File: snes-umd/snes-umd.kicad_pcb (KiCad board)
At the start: 2 copper layers, 20.3 x 96 mm, 4 parts, among them CON101 UMDv3-CONN, CON102 SNES-CONN, U101 MCP23008T-E_SS

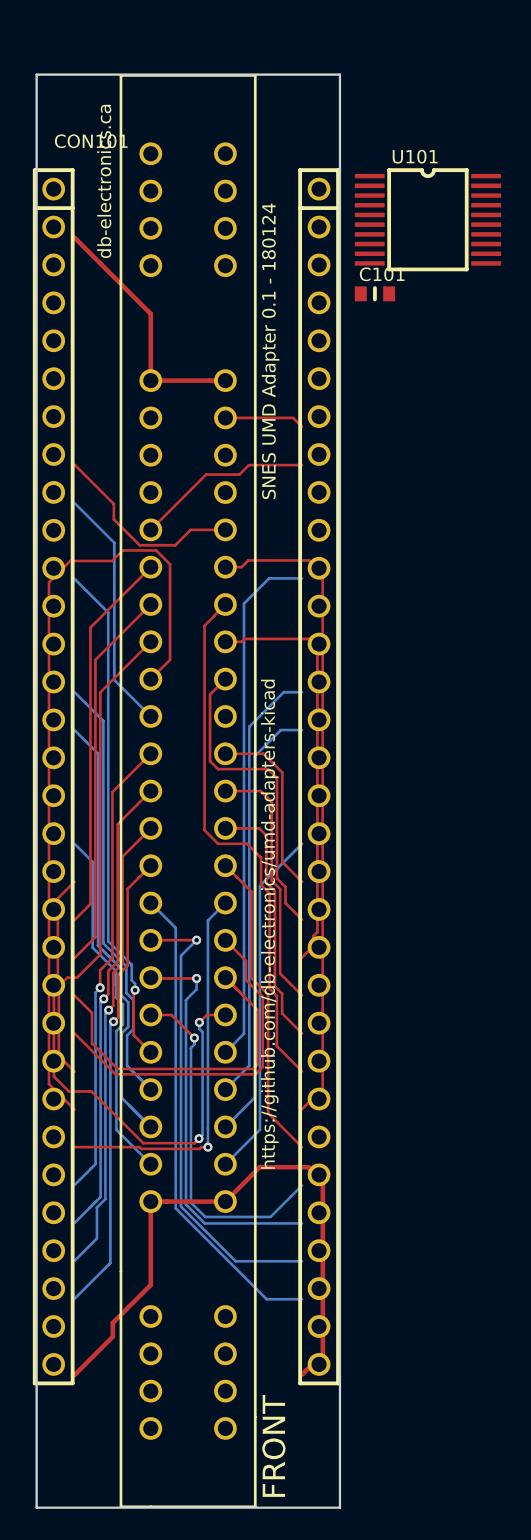
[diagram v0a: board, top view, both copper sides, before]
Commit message: board outline and sch mostly done
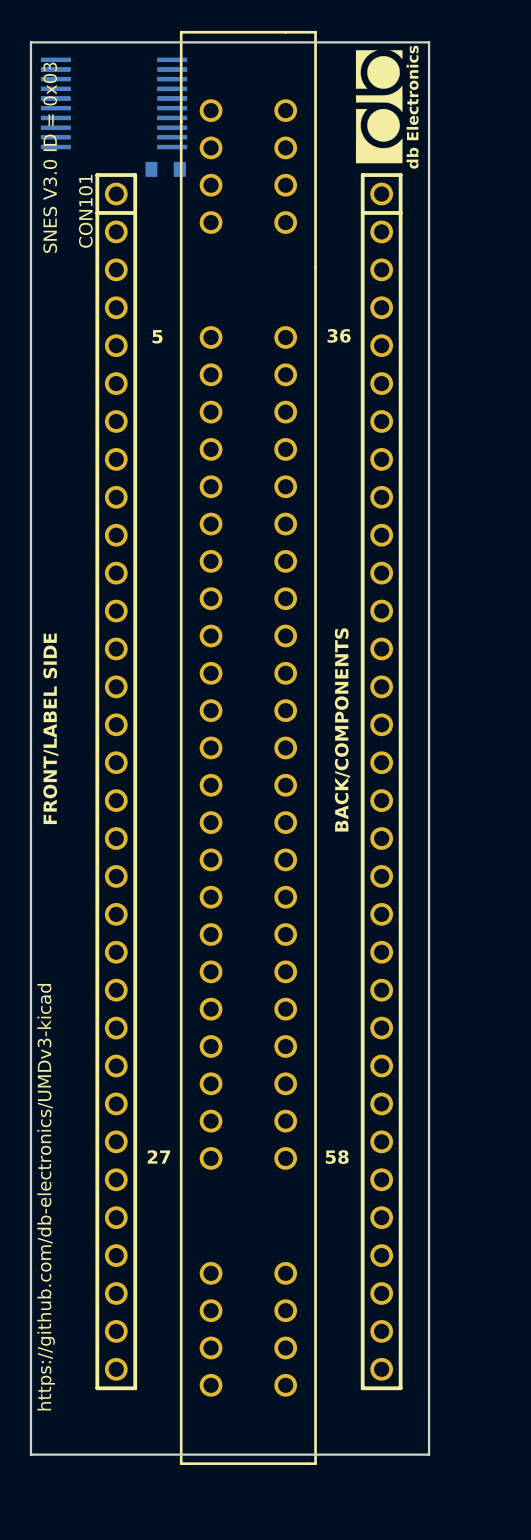
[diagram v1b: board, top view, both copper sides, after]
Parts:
- added logo101: logo, db-artwork:db-logo_7.5mm, F.Cu at (153.5, 60.2)
- C101, U101: moved to B.Cu
- moved CON102 88.3 mm to (142.2, 60.5), turned to 0 degrees
- moved U101 21.1 mm to (131.8, 62.9)
- moved C101 16.3 mm to (139.2, 64.4)
- moved CON101 4.21 mm to (135.9, 66.0)
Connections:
- CON102 pad 1: (no net) -> /CLK
- CON102 pad 18: (no net) -> /~{IRQ}
- CON102 pad 2: (no net) -> unconnected-(CON102-EXPAND-Pad2)
- CON102 pad 24: (no net) -> unconnected-(CON102-CIC_OUT-Pad24)
- CON102 pad 25: (no net) -> unconnected-(CON102-CIC_RST-Pad25)
- CON102 pad 27: +5V -> /5V_1
- CON102 pad 28: (no net) -> /D8
- CON102 pad 29: (no net) -> /D10
- CON102 pad 3: (no net) -> /D14
- CON102 pad 30: (no net) -> /D12
- CON102 pad 31: (no net) -> unconnected-(CON102-AUDIO_L-Pad31)
- CON102 pad 32: (no net) -> unconnected-(CON102-~{WRAM}-Pad32)
- CON102 pad 33: (no net) -> unconnected-(CON102-REFRESH-Pad33)
- CON102 pad 34: (no net) -> /D15
- CON102 pad 35: (no net) -> unconnected-(CON102-~{PAWR}-Pad35)
- CON102 pad 4: (no net) -> unconnected-(CON102-~{PARD}-Pad4)
- CON102 pad 55: (no net) -> unconnected-(CON102-CIC_IN-Pad55)
- CON102 pad 56: (no net) -> unconnected-(CON102-CIC_CLK-Pad56)
- CON102 pad 57: (no net) -> unconnected-(CON102-CPU_CLK-Pad57)
- CON102 pad 58: +5V -> /5V_1
- CON102 pad 59: (no net) -> /D9
- CON102 pad 60: (no net) -> /D11
- CON102 pad 61: (no net) -> /D13
- CON102 pad 62: (no net) -> unconnected-(CON102-AUDIO_R-Pad62)
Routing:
- net /D4: track 53.7 -> 0.00 mm
- net /D3: track 43.5 -> 0.00 mm
- net GND: track 40.1 -> 0.00 mm
- net /D2: track 35.7 -> 0.00 mm
- net /A7: track 35.3 -> 0.00 mm, vias 2 -> 0
- net /A8: track 35.2 -> 0.00 mm
- net /A15: track 33.9 -> 0.00 mm, vias 1 -> 0
- net /A13: track 33.3 -> 0.00 mm
- net /D5: track 32.2 -> 0.00 mm
- net /A19: track 32.1 -> 0.00 mm
- net /A22: track 31.7 -> 0.00 mm, vias 1 -> 0
- net /A20: track 31.1 -> 0.00 mm, vias 1 -> 0
- net /A21: track 31.1 -> 0.00 mm, vias 1 -> 0
- net /A14: track 31.0 -> 0.00 mm
- net /A23: track 31.0 -> 0.00 mm, vias 1 -> 0
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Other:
- board size 20.3 x 96 mm -> 26.7 x 94.6 mm
- rule pad_to_mask_clearance: 0.1016 -> 0
- board text added: "27"
- board text added: "36"
- board text added: "5"
- board text added: "58"
- board text added: "BACK/COMPONENTS"
- board text added: "FRONT/LABEL SIDE"
- board text added: "SNES V3.0 ID = 0x03"
- board text added: "db Electronics"
- board text added: "https://github.com/db-electronics/UMDv3-kicad"
- board text removed: "FRONT"
- board text removed: "SNES UMD Adapter 0.1 - 180124"
- board text removed: "db-electronics.ca"
- board text removed: "https://github.com/db-electronics/umd-adapters-kicad"

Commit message: layout almost complete
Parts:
- moved U101 0.28 mm to (132.1, 62.9)
- moved C101 0.25 mm to (138.9, 64.4)
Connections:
- CON101 pad 24: unconnected-(CON101A-~{CE0}-Pad24) -> /~{CE}
- CON101 pad 4: unconnected-(CON101A-MOSI/IO6-Pad4) -> /EXPAND
- CON101 pad 46: unconnected-(CON101B-D9-Pad46) -> /D9
- CON101 pad 47: unconnected-(CON101B-D11-Pad47) -> /D11
- CON101 pad 49: unconnected-(CON101B-D13-Pad49) -> /D13
- CON101 pad 5: unconnected-(CON101A-SCK/IO4-Pad5) -> /~{PARD}
- CON101 pad 50: unconnected-(CON101B-D15-Pad50) -> /D15
- CON101 pad 60: unconnected-(CON101B-NSS/IO5-Pad60) -> /~{PAWR}
- CON101 pad 61: unconnected-(CON101B-MISO/IO7-Pad61) -> /REFRESH
- CON101 pad 62: unconnected-(CON101B-IO8-Pad62) -> /~{WRAM}
- CON102 pad 2: unconnected-(CON102-EXPAND-Pad2) -> /EXPAND
- CON102 pad 32: unconnected-(CON102-~{WRAM}-Pad32) -> /~{WRAM}
- CON102 pad 33: unconnected-(CON102-REFRESH-Pad33) -> /REFRESH
- CON102 pad 35: unconnected-(CON102-~{PAWR}-Pad35) -> /~{PAWR}
- CON102 pad 4: unconnected-(CON102-~{PARD}-Pad4) -> /~{PARD}
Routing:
- net /A19: track 0.00 -> 54.1 mm, vias 0 -> 1
- net /~{RD}: track 0.00 -> 53.4 mm
- net /D12: track 0.00 -> 52.1 mm
- net /D10: track 0.00 -> 50.2 mm
- net /A20: track 0.00 -> 49.5 mm, vias 0 -> 1
- net /D8: track 0.00 -> 49.0 mm
- net /A23: track 0.00 -> 47.1 mm
- net /A4: track 0.00 -> 44.7 mm
- net /D13: track 0.00 -> 44.1 mm, vias 0 -> 1
- net /A21: track 0.00 -> 42.9 mm, vias 0 -> 1
- net /A0: track 0.00 -> 42.8 mm
- net /D14: track 0.00 -> 42.6 mm
- net /D15: track 0.00 -> 42.6 mm
- net /A22: track 0.00 -> 42.4 mm
- net /A2: track 0.00 -> 42.0 mm
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- added copper zone on B.Cu, net GND
- added copper zone on F.Cu, net GND
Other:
- board text added: "SNES v3.0 ID = 0x03"
- board text removed: "SNES V3.0 ID = 0x03"

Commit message: version 3.0 files
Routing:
- net /D11: track 37.7 -> 36.7 mm
- net /D5: track 7.96 -> 8.84 mm
- net /A15: track 13.2 -> 13.8 mm
- net /~{RD}: track 53.4 -> 52.8 mm
- net /D3: track 26.2 -> 25.6 mm
- net /D8: track 49.0 -> 48.5 mm
- net /D12: track 52.1 -> 51.6 mm
- net GND: vias 10 -> 14
